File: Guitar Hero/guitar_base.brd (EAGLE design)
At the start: 50.8 x 54.6 mm, 5 parts

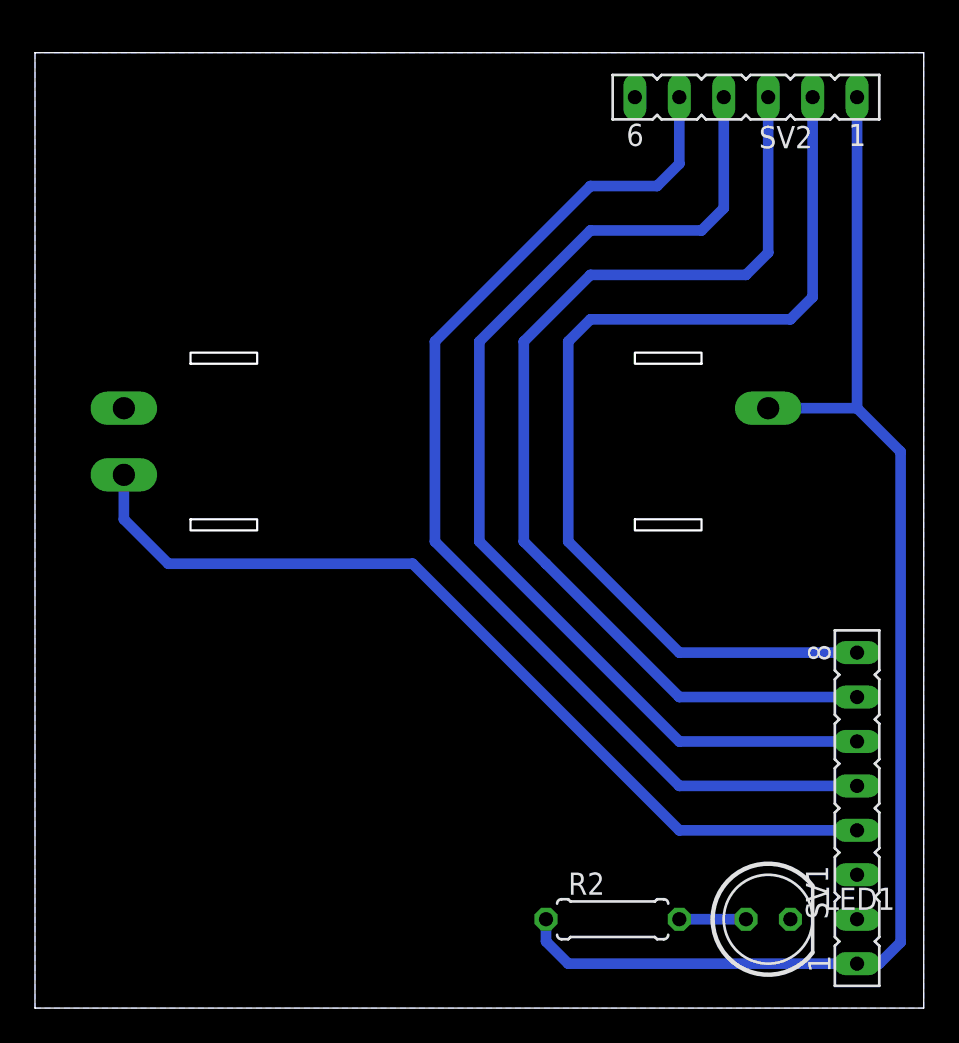
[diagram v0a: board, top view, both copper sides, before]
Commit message: Nano++ schematic; guitar hero redo to not use 1/64th bit
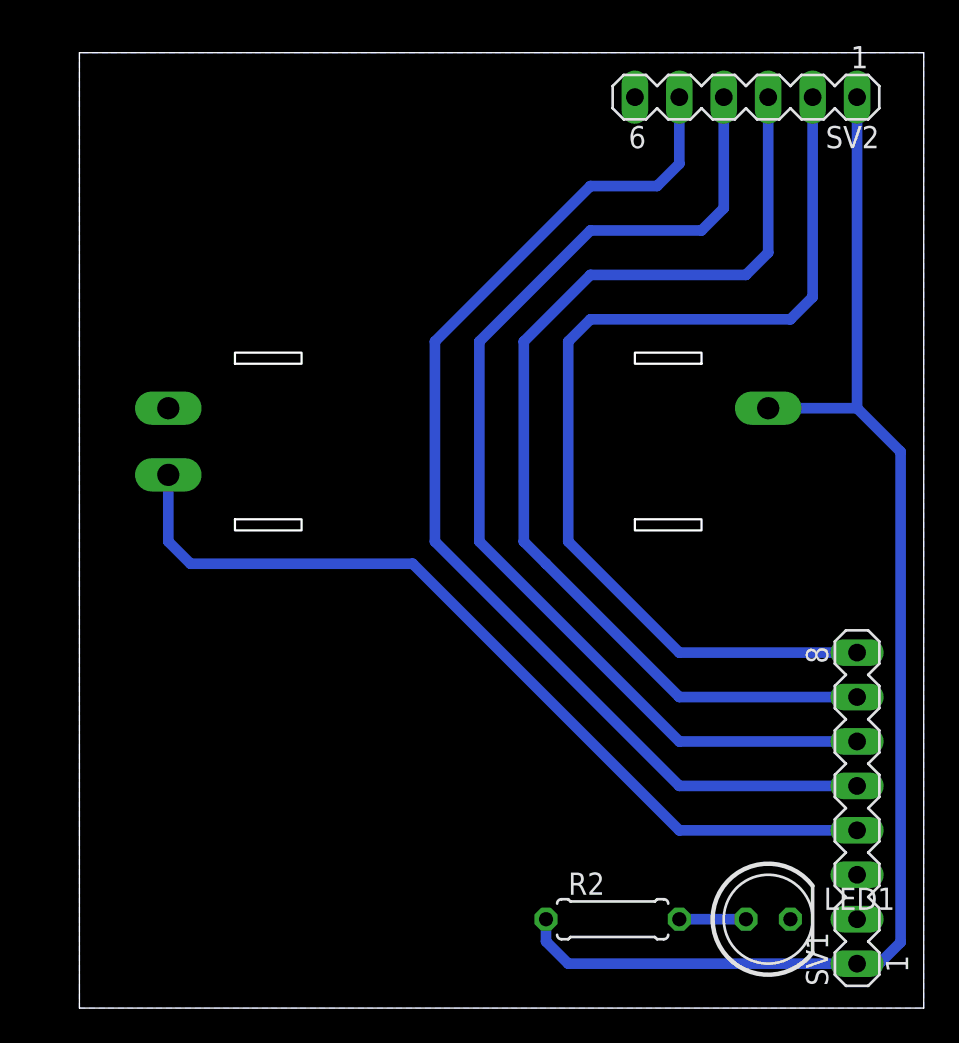
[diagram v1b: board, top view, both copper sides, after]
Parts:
- SV1: device con-lsta:FE08 -> con-lstb:MA08-1
- SV2: device con-lsta:FE06 -> con-lstb:MA06-1
- moved U$1 2.54 mm to (40.6, 44.5)
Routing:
- net POT: track 51.8 -> 50.0 mm
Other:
- board size 50.8 x 54.6 mm -> 48.3 x 54.6 mm
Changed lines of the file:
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@@
 <board>
 <plain>
-<wire x1="33.02" y1="13.97" x2="83.82" y2="13.97" width="0" layer="20"/>
+<wire x1="35.56" y1="13.97" x2="83.82" y2="13.97" width="0" layer="20"/>
 <wire x1="83.82" y1="13.97" x2="83.82" y2="68.58" width="0" layer="20"/>
-<wire x1="83.82" y1="68.58" x2="33.02" y2="68.58" width="0" layer="20"/>
-<wire x1="33.02" y1="68.58" x2="33.02" y2="13.97" width="0" layer="20"/>
+<wire x1="83.82" y1="68.58" x2="35.56" y2="68.58" width="0" layer="20"/>
+<wire x1="35.56" y1="68.58" x2="35.56" y2="13.97" width="0" layer="20"/>
 </plain>
 <attributes>
@@
 <element name="LED1" library="led" library_urn="urn:adsk.eagle:library:259" package="LED5MM" package3d_urn="urn:adsk.eagle:package:15799/1" value="" x="74.93" y="19.05"/>
 <element name="R2" library="rcl" library_urn="urn:adsk.eagle:library:334" package="0207/7" package3d_urn="urn:adsk.eagle:package:23493/1" value="" x="66.04" y="19.05"/>
-<element name="SV1" library="con-lsta" library_urn="urn:adsk.eagle:library:161" package="FE08" package3d_urn="urn:adsk.eagle:package:8194/1" value="" x="80.01" y="25.4" rot="R90">
+<element name="SV1" library="con-lstb" library_urn="urn:adsk.eagle:library:162" package="MA08-1" package3d_urn="urn:adsk.eagle:package:8343/1" value="" x="80.01" y="25.4" rot="R90">
 <attribute name="MF" value="" x="80.01" y="25.4" size="1.778" layer="27" rot="R90" display="off"/>
 <attribute name="MPN" value="" x="80.01" y="25.4" size="1.778" layer="27" rot="R90" display="off"/>
@@
 <attribute name="OC_NEWARK" value="unknown" x="80.01" y="25.4" size="1.778" layer="27" rot="R90" display="off"/>
 </element>
-<element name="SV2" library="con-lsta" library_urn="urn:adsk.eagle:library:161" package="FE06" package3d_urn="urn:adsk.eagle:package:8191/1" value="" x="73.66" y="66.04" rot="R180">
+<element name="SV2" library="con-lstb" library_urn="urn:adsk.eagle:library:162" package="MA06-1" package3d_urn="urn:adsk.eagle:package:8340/1" value="" x="73.66" y="66.04" rot="R180">
 <attribute name="MF" value="" x="73.66" y="66.04" size="1.778" layer="27" rot="R180" display="off"/>
 <attribute name="MPN" value="" x="73.66" y="66.04" size="1.778" layer="27" rot="R180" display="off"/>
@@
 <attribute name="OC_NEWARK" value="unknown" x="73.66" y="66.04" size="1.778" layer="27" rot="R180" display="off"/>
 </element>
-<element name="U$1" library="319k" package="SLIDE-POT" value="SLIDE-POT" x="38.1" y="44.45" rot="R180"/>
+<element name="U$1" library="319k" package="SLIDE-POT" value="SLIDE-POT" x="40.64" y="44.45" rot="R180"/>
 </elements>
 <signals>
@@
 <signal name="POT">
 <contactref element="SV1" pad="4"/>
+<wire x1="80.01" y1="24.13" x2="69.85" y2="24.13" width="0.6096" layer="16"/>
+<wire x1="69.85" y1="24.13" x2="54.61" y2="39.37" width="0.6096" layer="16"/>
 <contactref element="U$1" pad="OUT"/>
-<wire x1="80.01" y1="24.13" x2="69.85" y2="24.13" width="0.6096" layer="16"/>
-<wire x1="54.61" y1="39.37" x2="40.64" y2="39.37" width="0.6096" layer="16"/>
-<wire x1="40.64" y1="39.37" x2="38.1" y2="41.91" width="0.6096" layer="16"/>
-<wire x1="38.1" y1="41.91" x2="38.1" y2="44.45" width="0.6096" layer="16"/>
-<wire x1="69.85" y1="24.13" x2="54.61" y2="39.37" width="0.6096" layer="16"/>
+<wire x1="54.61" y1="39.37" x2="41.91" y2="39.37" width="0.6096" layer="16"/>
+<wire x1="41.91" y1="39.37" x2="40.64" y2="40.64" width="0.6096" layer="16"/>
+<wire x1="40.64" y1="40.64" x2="40.64" y2="44.45" width="0.6096" layer="16"/>
 </signal>
 <signal name="GND">
 <contactref element="SV1" pad="2"/>
 <contactref element="LED1" pad="K"/>
-<contactref element="U$1" pad="IN2"/>
 <contactref element="SV2" pad="6"/>
 <polygon width="0.6096" layer="16" isolate="1.27">
-<vertex x="33.02" y="68.58"/>
-<vertex x="33.02" y="13.97"/>
+<vertex x="35.56" y="68.58"/>
+<vertex x="35.56" y="13.97"/>
 <vertex x="83.82" y="13.97"/>
 <vertex x="83.82" y="68.58"/>
 </polygon>
+<contactref element="U$1" pad="IN2"/>
 </signal>
 <signal name="VCC">
 <contactref element="SV1" pad="1"/>
 <contactref element="R2" pad="1"/>
-<contactref element="U$1" pad="IN1"/>
 <contactref element="SV2" pad="1"/>
 <wire x1="80.01" y1="16.51" x2="81.28" y2="16.51" width="0.6096" layer="16"/>
 <wire x1="81.28" y1="16.51" x2="82.4992" y2="17.7292" width="0.6096" layer="16"/>
 <wire x1="82.4992" y1="17.7292" x2="82.4992" y2="45.7708" width="0.6096" layer="16"/>
-<wire x1="80.01" y1="48.26" x2="82.4992" y2="45.7708" width="0.6096" layer="16"/>
+<wire x1="82.4992" y1="45.7708" x2="80.01" y2="48.26" width="0.6096" layer="16"/>
 <wire x1="80.01" y1="48.26" x2="80.01" y2="66.04" width="0.6096" layer="16"/>
-<wire x1="74.93" y1="48.26" x2="80.01" y2="48.26" width="0.6096" layer="16"/>
 <wire x1="62.23" y1="19.05" x2="62.23" y2="17.78" width="0.6096" layer="16"/>
 <wire x1="62.23" y1="17.78" x2="63.5" y2="16.51" width="0.6096" layer="16"/>
 <wire x1="63.5" y1="16.51" x2="80.01" y2="16.51" width="0.6096" layer="16"/>
+<contactref element="U$1" pad="IN1"/>
+<wire x1="80.01" y1="48.26" x2="74.93" y2="48.26" width="0.6096" layer="16"/>
 </signal>
 <signal name="N$1">
